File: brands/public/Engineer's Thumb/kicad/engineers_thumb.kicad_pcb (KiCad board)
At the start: 2 copper layers, 43 parts, among them CN1 IN, CN2 OUT, IC1 TL072, IC2 TL072, IC3 CA3080, P1 1M Lin, P2 1M Log, P3 1M Lin, P4 10k Log, Q1 BC327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

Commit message: Engineer's Thumb pcb
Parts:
- added switch_3pdt_stomp_onboard: VAL**, drow:switch_3pdt_stomp_onboard, F.Cu at (43.8, 106.2)
- moved B1 296.5 mm to (67.0, 106.5)
- moved CN2 282.6 mm to (26.0, 83.5)
- moved IC1 264.4 mm to (92.2, 69.8)
- moved IC3 262.4 mm to (92.2, 53.4)
- moved R7 256.3 mm to (102.0, 79.3)
- moved CN1 255.9 mm to (72.0, 100.0), turned to 180 degrees
- moved SW1 251.2 mm to (102.5, 41.0)
- moved P1 248.7 mm to (108.6, 73.6)
- moved R14 246.7 mm to (111.8, 79.3)
- moved D5 239.4 mm to (117.6, 70.8)
- moved IC2 238.5 mm to (115.2, 40.0)
- moved R10 236.7 mm to (121.6, 77.0)
- moved D2 235.9 mm to (119.1, 56.4)
- moved R8 229.9 mm to (127.4, 71.8)
- moved D1 229.6 mm to (125.8, 59.4)
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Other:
- board outline added: 61 x 100 mm
- net class Default: clearance 0.254 -> 0.4; trace_width 0.254 -> 0.6; via_dia 0.889 -> 0.8; via_drill 0.635 -> 0.7
- rule trace_clearance: 0.254 -> 0.4
- rule via_min_size: 0.889 -> 0.8

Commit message: Engineer's Thumb
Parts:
- CN1: footprint drow:socket_jack-6.35_onboard -> drow:socket_jack_powered-6.35_onboard
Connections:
- CN1 pad 2: /V- -> GND
- CN1 pad 3: GND -> /V-
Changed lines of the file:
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@@
-(kicad_pcb (version 4) (host pcbnew "(2014-jul-16 BZR unknown)-product")
+(kicad_pcb (version 4) (host pcbnew 0.201411291501+5307~19~ubuntu14.04.1-product)
   (general
-    (links 80)
-    (no_connects 80)
-    (area 20.949999 20.949999 174.864 122.775)
+    (links 87)
+    (no_connects 87)
+    (area 20.949999 20.949999 82.050001 121.050001)
     (thickness 1.6)
     (drawings 7)
@@
       (net 6 "Net-(C2-Pad1)"))
   )
-  (module drow:socket_jack-6.35_onboard locked (layer F.Cu)
-    (at 72 100 180)
-    (fp_text reference CN1 (at 6 20 180) (layer F.SilkS)
-      (effects (font (size 1.5 1.5) (thickness 0.15)))
-    )
-    (fp_text value IN (at 6.5 8.5 180) (layer F.SilkS)
-      (effects (font (size 1.5 1.5) (thickness 0.15)))
-    )
-    (fp_line (start 16.7 3.75) (end 20.7 3.75) (layer F.SilkS) (width 0.15))
-    (fp_line (start 20.7 3.75) (end 20.7 12.75) (layer F.SilkS) (width 0.15))
-    (fp_line (start 20.7 12.75) (end 16.7 12.75) (layer F.SilkS) (width 0.15))
-    (fp_line (start 16.7 -1.75) (end -4 -1.75) (layer F.SilkS) (width 0.15))
-    (fp_line (start -4 -1.75) (end -4 18.25) (layer F.SilkS) (width 0.15))
-    (fp_line (start -4 18.25) (end 16.7 18.25) (layer F.SilkS) (width 0.15))
-    (fp_line (start 16.7 18.25) (end 16.7 -1.75) (layer F.SilkS) (width 0.15))
-    (pad 1 thru_hole circle (at 0 0 180) (size 3.5 3.5) (drill 1.5) (layers *.Cu *.Mask)
-      (net 15 "Net-(CN1-Pad1)"))
-    (pad 2 thru_hole circle (at 6.35 0 180) (size 3.5 3.5) (drill 1.5) (layers *.Cu *.Mask)
-      (net 1 /V-))
-    (pad 3 thru_hole circle (at 12.7 0 180) (size 3.5 3.5) (drill 1.5) (layers *.Cu *.Mask)
-      (net 7 GND))
-    (pad 4 thru_hole circle (at 0 16.5 180) (size 3.5 3.5) (drill 1.5) (layers *.Cu *.Mask))
-    (pad 5 thru_hole circle (at 6.35 16.5 180) (size 3.5 3.5) (drill 1.5) (layers *.Cu *.Mask))
-    (pad 6 thru_hole circle (at 12.7 16.5 180) (size 3.5 3.5) (drill 1.5) (layers *.Cu *.Mask))
-  )
-  (module drow:socket_jack-6.35_onboard locked (layer F.Cu)
-    (at 26 83.5)
-    (fp_text reference CN2 (at 6 20) (layer F.SilkS)
-      (effects (font (size 1.5 1.5) (thickness 0.15)))
-    )
-    (fp_text value OUT (at 6.5 8.5) (layer F.SilkS)
-      (effects (font (size 1.5 1.5) (thickness 0.15)))
-    )
-    (fp_line (start 16.7 3.75) (end 20.7 3.75) (layer F.SilkS) (width 0.15))
-    (fp_line (start 20.7 3.75) (end 20.7 12.75) (layer F.SilkS) (width 0.15))
-    (fp_line (start 20.7 12.75) (end 16.7 12.75) (layer F.SilkS) (width 0.15))
-    (fp_line (start 16.7 -1.75) (end -4 -1.75) (layer F.SilkS) (width 0.15))
-    (fp_line (start -4 -1.75) (end -4 18.25) (layer F.SilkS) (width 0.15))
-    (fp_line (start -4 18.25) (end 16.7 18.25) (layer F.SilkS) (width 0.15))
-    (fp_line (start 16.7 18.25) (end 16.7 -1.75) (layer F.SilkS) (width 0.15))
-    (pad 1 thru_hole circle (at 0 0) (size 3.5 3.5) (drill 1.5) (layers *.Cu *.Mask)
-      (net 16 "Net-(CN2-Pad1)"))
-    (pad 2 thru_hole circle (at 6.35 0) (size 3.5 3.5) (drill 1.5) (layers *.Cu *.Mask)
-      (net 7 GND))
-    (pad 3 thru_hole circle (at 12.7 0) (size 3.5 3.5) (drill 1.5) (layers *.Cu *.Mask))
-    (pad 4 thru_hole circle (at 0 16.5) (size 3.5 3.5) (drill 1.5) (layers *.Cu *.Mask))
-    (pad 5 thru_hole circle (at 6.35 16.5) (size 3.5 3.5) (drill 1.5) (layers *.Cu *.Mask))
-    (pad 6 thru_hole circle (at 12.7 16.5) (size 3.5 3.5) (drill 1.5) (layers *.Cu *.Mask))
-  )
   (module drow:diode_light_2.5mm (layer F.Cu)
     (at 125.82064 59.429)
@@
     (pad 9 thru_hole circle (at 10.6 9.4) (size 3.2 3.2) (drill 1.5) (layers *.Cu *.Mask F.SilkS))
   )
+  (module drow:socket_jack_powered-6.35_onboard (layer F.Cu)
+    (at 72 100 180)
+    (fp_text reference CN1 (at 6 20 180) (layer F.SilkS)
+      (effects (font (size 1.5 1.5) (thickness 0.15)))
+    )
+    (fp_text value IN (at 6.5 8.5 180) (layer F.SilkS)
+      (effects (font (size 1.5 1.5) (thickness 0.15)))
+    )
+    (fp_line (start 16.7 3.75) (end 20.7 3.75) (layer F.SilkS) (width 0.15))
+    (fp_line (start 20.7 3.75) (end 20.7 12.75) (layer F.SilkS) (width 0.15))
+    (fp_line (start 20.7 12.75) (end 16.7 12.75) (layer F.SilkS) (width 0.15))
+    (fp_line (start 16.7 -1.75) (end -4 -1.75) (layer F.SilkS) (width 0.15))
+    (fp_line (start -4 -1.75) (end -4 18.25) (layer F.SilkS) (width 0.15))
+    (fp_line (start -4 18.25) (end 16.7 18.25) (layer F.SilkS) (width 0.15))
+    (fp_line (start 16.7 18.25) (end 16.7 -1.75) (layer F.SilkS) (width 0.15))
+    (pad 2 thru_hole circle (at 0 0 180) (size 3.5 3.5) (drill 1.5) (layers *.Cu *.Mask F.SilkS)
+      (net 7 GND))
+    (pad 3 thru_hole circle (at 6.35 0 180) (size 3.5 3.5) (drill 1.5) (layers *.Cu *.Mask F.SilkS)
+      (net 1 /V-))
+    (pad 2 thru_hole circle (at 12.7 0 180) (size 3.5 3.5) (drill 1.5) (layers *.Cu *.Mask F.SilkS)
+      (net 7 GND))
+    (pad 2 thru_hole circle (at 0 16.5 180) (size 3.5 3.5) (drill 1.5) (layers *.Cu *.Mask F.SilkS)
+      (net 7 GND))
+    (pad 3 thru_hole circle (at 6.35 16.5 180) (size 3.5 3.5) (drill 1.5) (layers *.Cu *.Mask F.SilkS)
+      (net 1 /V-))
+    (pad 1 thru_hole circle (at 12.7 16.5 180) (size 3.5 3.5) (drill 1.5) (layers *.Cu *.Mask F.SilkS)
+      (net 15 "Net-(CN1-Pad1)"))
+  )
+  (module drow:socket_jack-6.35_onboard (layer F.Cu)
+    (at 26 83.5)
+    (fp_text reference CN2 (at 6 20) (layer F.SilkS)
+      (effects (font (size 1.5 1.5) (thickness 0.15)))
+    )
+    (fp_text value OUT (at 6.5 8.5) (layer F.SilkS)
+      (effects (font (size 1.5 1.5) (thickness 0.15)))
+    )
+    (fp_line (start 16.7 3.75) (end 20.7 3.75) (layer F.SilkS) (width 0.15))
+    (fp_line (start 20.7 3.75) (end 20.7 12.75) (layer F.SilkS) (width 0.15))
+    (fp_line (start 20.7 12.75) (end 16.7 12.75) (layer F.SilkS) (width 0.15))
+    (fp_line (start 16.7 -1.75) (end -4 -1.75) (layer F.SilkS) (width 0.15))
+    (fp_line (start -4 -1.75) (end -4 18.25) (layer F.SilkS) (width 0.15))
+    (fp_line (start -4 18.25) (end 16.7 18.25) (layer F.SilkS) (width 0.15))
+    (fp_line (start 16.7 18.25) (end 16.7 -1.75) (layer F.SilkS) (width 0.15))
+    (pad 2 thru_hole circle (at 0 0) (size 3.5 3.5) (drill 1.5) (layers *.Cu *.Mask F.SilkS)
+      (net 7 GND))
+    (pad 2 thru_hole circle (at 6.35 0) (size 3.5 3.5) (drill 1.5) (layers *.Cu *.Mask F.SilkS)
+      (net 7 GND))
+    (pad 2 thru_hole circle (at 12.7 0) (size 3.5 3.5) (drill 1.5) (layers *.Cu *.Mask F.SilkS)
+      (net 7 GND))
+    (pad 2 thru_hole circle (at 0 16.5) (size 3.5 3.5) (drill 1.5) (layers *.Cu *.Mask F.SilkS)
+      (net 7 GND))
+    (pad 2 thru_hole circle (at 6.35 16.5) (size 3.5 3.5) (drill 1.5) (layers *.Cu *.Mask F.SilkS)
+      (net 7 GND))
+    (pad 1 thru_hole circle (at 12.7 16.5) (size 3.5 3.5) (drill 1.5) (layers *.Cu *.Mask F.SilkS)
+      (net 16 "Net-(CN2-Pad1)"))
+  )
   (gr_line (start 39 111) (end 82 111) (angle 90) (layer Edge.Cuts) (width 0.1))

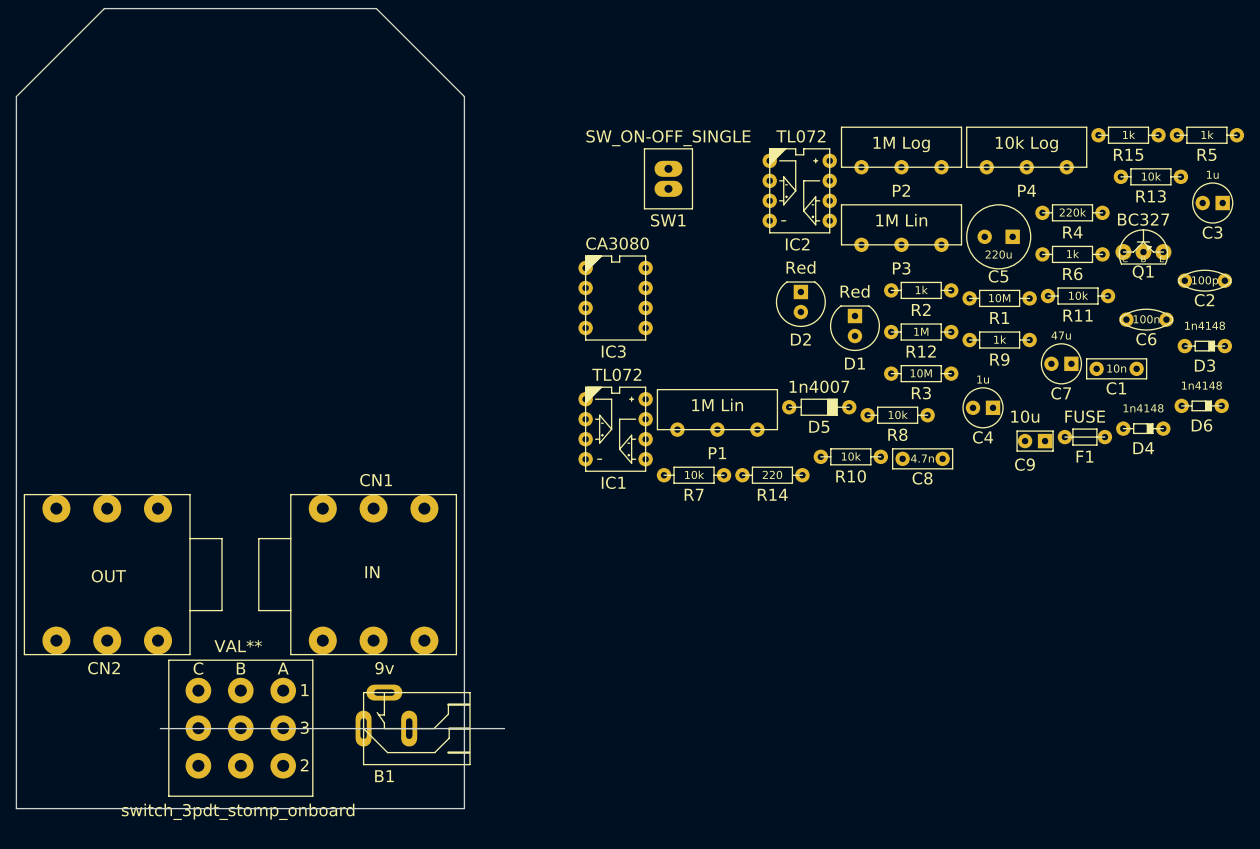
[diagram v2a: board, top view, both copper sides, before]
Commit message: Engineer's Thumb, added 3PDT switch to KiCAD lib
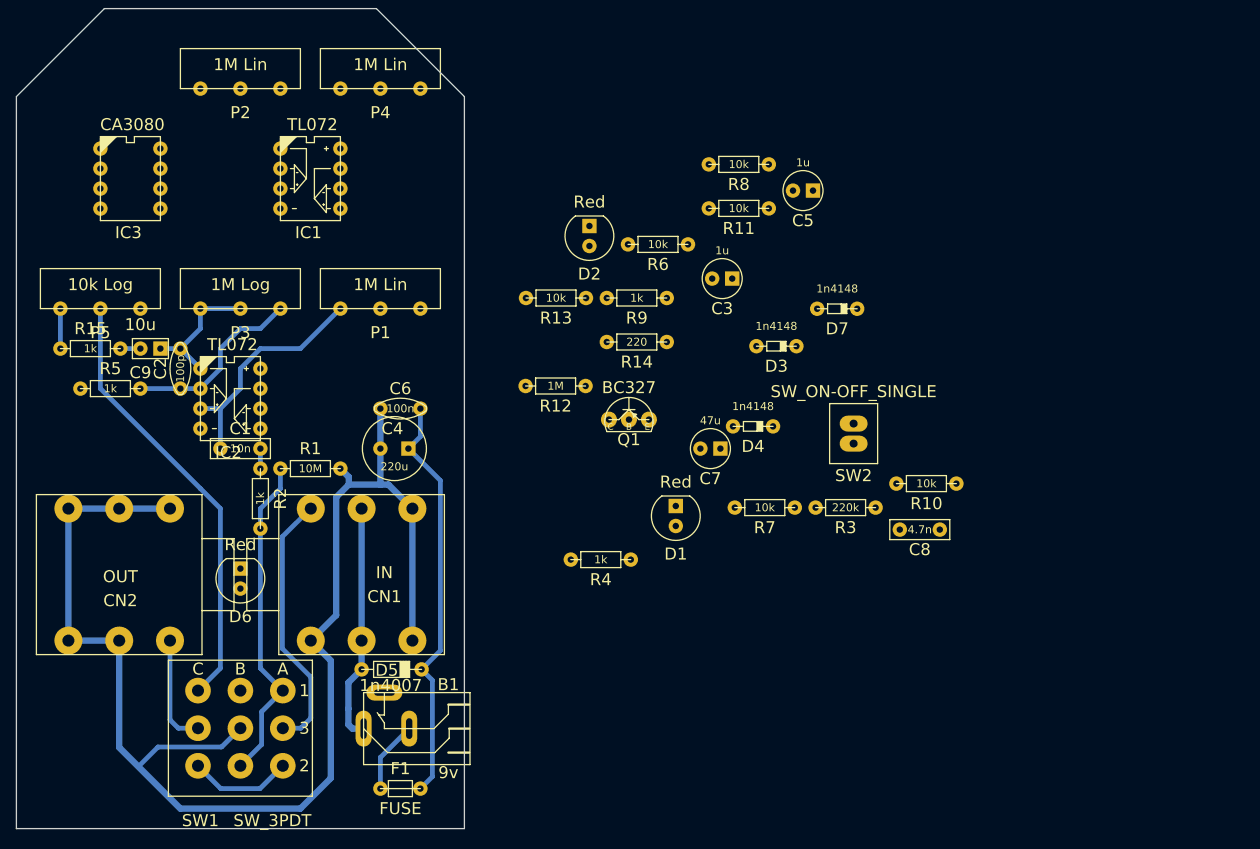
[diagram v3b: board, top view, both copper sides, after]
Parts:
- removed switch_3pdt_stomp_onboard: VAL**, drow:switch_3pdt_stomp_onboard
- added D7: 1n4148, drow:diode_5mm, F.Cu at (121.1, 58.5)
- added P5: 10k Log, drow:potentiometer_panel_5mm, F.Cu at (31.5, 58.5)
- added SW2: SW_ON-OFF_SINGLE, drow:socket_2pin_2.5mm, F.Cu at (125.7, 72.9)
- C4: value 1u -> 220u; footprint drow:capacitor_2.5mm_electrolytic_5mm -> drow:capacitor_3.5mm_electrolytic_8mm
- C5: value 220u -> 1u; footprint drow:capacitor_3.5mm_electrolytic_8mm -> drow:capacitor_2.5mm_electrolytic_5mm
- D6: value 1n4148 -> Red; footprint drow:diode_5mm -> drow:diode_light_2.5mm
- P2: value 1M Log -> 1M Lin
- P3: value 1M Lin -> 1M Log
- P4: value 10k Log -> 1M Lin
- R3: value 10M -> 220k
- R4: value 220k -> 1k
- R6: value 1k -> 10k
- SW1: value SW_ON-OFF_SINGLE -> SW_3PDT; footprint drow:socket_2pin_2.5mm -> drow:switch_3pdt_stomp_onboard
- moved R5 133.4 mm to (36.5, 68.5), turned to 180 degrees
- moved C2 125.8 mm to (41.5, 63.5), turned to 270 degrees
- moved R15 125.1 mm to (34.0, 63.5), turned to 180 degrees
- moved D6 119.4 mm to (49.0, 91.0)
- moved C9 111.2 mm to (36.5, 63.5)
- moved C1 105.0 mm to (51.5, 76.0), turned to 180 degrees
- moved F1 91.8 mm to (71.5, 118.5), turned to 180 degrees
- moved C6 89.0 mm to (71.5, 71.0), turned to 180 degrees
- moved SW1 87.8 mm to (43.7, 106.2)
- moved R2 84.3 mm to (51.5, 86.0), turned to 90 degrees
- moved P2 83.2 mm to (49.0, 31.0)
- moved P3 83.0 mm to (49.0, 58.5)
- moved R1 81.5 mm to (61.5, 78.5), turned to 180 degrees
- moved P4 81.4 mm to (66.5, 31.0)
- moved R13 75.9 mm to (84.7, 57.2)
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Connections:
- C4 pad 2: Net-(C4-Pad2) -> +9V
- C5 pad 2: +9V -> Net-(C5-Pad2)
- D5 pad 1: GND -> /V-
- D6 pad 2: Net-(D6-Pad2) -> /Led
- IC1 pad 3: Net-(C1-Pad2) -> Net-(IC1-Pad3)
- IC1 pad 5: Net-(C1-Pad2) -> Net-(C5-Pad2)
- IC1 pad 6: Net-(C2-Pad2) -> Net-(D7-Pad2)
- IC1 pad 7: Net-(C2-Pad1) -> Net-(D7-Pad1)
- IC2 pad 1: Net-(D6-Pad1) -> Net-(C2-Pad1)
- IC2 pad 2: Net-(D6-Pad2) -> Net-(C2-Pad2)
- IC2 pad 3: Net-(C4-Pad2) -> Net-(C1-Pad2)
- IC2 pad 6: +9V -> Net-(IC2-Pad6)
- IC3 pad 2: +9V -> Net-(IC3-Pad2)
- P1 pad 2: Net-(D3-Pad2) -> Net-(IC1-Pad3)
- P1 pad 3: Net-(D3-Pad2) -> Net-(C1-Pad2)
- P2 pad 1: Net-(C2-Pad2) -> Net-(P2-Pad1)
- P2 pad 2: Net-(C2-Pad1) -> Net-(D3-Pad2)
- P2 pad 3: Net-(C2-Pad1) -> Net-(D3-Pad2)
- P3 pad 1: Net-(C3-Pad2) -> Net-(C2-Pad2)
- P3 pad 2: Net-(D4-Pad1) -> Net-(C2-Pad1)
- P3 pad 3: Net-(D4-Pad1) -> Net-(C2-Pad1)
- P4 pad 1: GND -> Net-(C3-Pad2)
- P4 pad 2: Net-(CN2-Pad1) -> Net-(D4-Pad1)
- P4 pad 3: Net-(P4-Pad3) -> Net-(D4-Pad1)
- Q1 pad 2: Net-(D6-Pad1) -> Net-(D7-Pad1)
- Q1 pad 3: Net-(D6-Pad2) -> Net-(D7-Pad2)
- R1 pad 2: Net-(CN1-Pad1) -> /In
- R10 pad 2: +9V -> Net-(R10-Pad2)
- R12 pad 2: +9V -> Net-(R12-Pad2)
- R14 pad 2: +9V -> Net-(R14-Pad2)
- R15 pad 2: Net-(P4-Pad3) -> Net-(P5-Pad3)
- R2 pad 1: Net-(CN1-Pad1) -> /In
- R3 pad 1: +9V -> Net-(P2-Pad1)
- R3 pad 2: Net-(C1-Pad2) -> Net-(C3-Pad2)
- R4 pad 1: Net-(P1-Pad1) -> Net-(C3-Pad2)
- R4 pad 2: Net-(C3-Pad2) -> Net-(C5-Pad2)
- R5 pad 1: Net-(C3-Pad2) -> Net-(C2-Pad2)
- R5 pad 2: Net-(C4-Pad2) -> Net-(IC3-Pad6)
- R6 pad 1: Net-(C2-Pad2) -> +9V
- R6 pad 2: Net-(IC3-Pad6) -> Net-(D6-Pad1)
- R9 pad 1: +9V -> Net-(R12-Pad2)
- R9 pad 2: Net-(D6-Pad2) -> Net-(D7-Pad2)
- SW1 pad 1: Net-(C8-Pad2) -> /Out
- SW1 pad 2: +9V -> Net-(SW1-Pad2)
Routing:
- net GND: track 0.00 -> 172.2 mm
- net /Out: track 0.00 -> 55.1 mm
- net +9V: track 0.00 -> 51.9 mm
- net /In: track 0.00 -> 41.5 mm
- net Net-(CN1-Pad1): track 0.00 -> 33.2 mm
- net /V-: track 0.00 -> 29.8 mm
- net Net-(C1-Pad2): track 0.00 -> 29.1 mm
- net Net-(C2-Pad2): track 0.00 -> 23.1 mm
- net Net-(C2-Pad1): track 0.00 -> 17.1 mm
- net Net-(CN2-Pad1): track 0.00 -> 13.8 mm
- net Net-(SW1-Pad2): track 0.00 -> 13.0 mm
- net Net-(B1-Pad1): track 0.00 -> 8.99 mm
- net Net-(P5-Pad3): track 0.00 -> 5.00 mm
- net Net-(C9-Pad1): track 0.00 -> 2.50 mm
- net Net-(C1-Pad1): track 0.00 -> 2.50 mm
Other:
- board size 61 x 100 mm -> 56 x 102.5 mm
- net class gnd added: clearance 0.4, trace_width 0.8, via_dia 0.8, via_drill 0.7
